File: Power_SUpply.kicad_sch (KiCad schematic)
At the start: 6 parts, among them J1 Conn_01x02, J2 Conn_01x02, U1 L7805

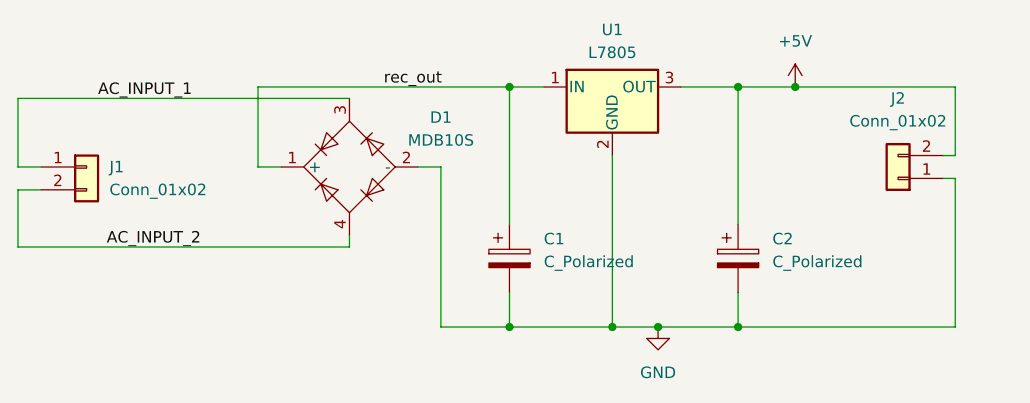
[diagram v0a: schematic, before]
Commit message: changed the connector
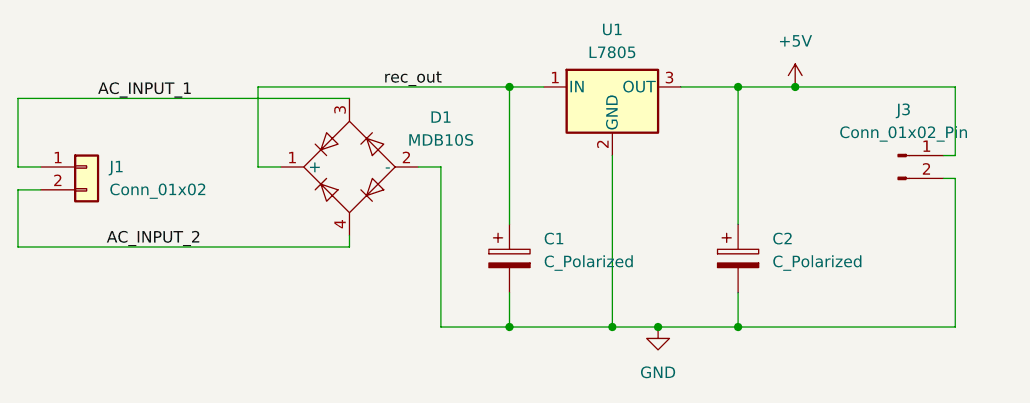
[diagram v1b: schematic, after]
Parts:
- removed J2: Conn_01x02, TerminalBlock_Phoenix:TerminalBlock_Phoenix_MKDS-1,5-2_1x02_P5.00mm_Horizontal, symbol Connector_Generic:Conn_01x02
- added J3: Conn_01x02_Pin, symbol Connector:Conn_01x02_Pin
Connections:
- net +5V: now also J3.1 (Pin_1)
- net GND: now also J3.2 (Pin_2)
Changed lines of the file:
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@@
-	)
-	(symbol
-		(lib_id "Connector_Generic:Conn_01x02")
-		(at 177.8 97.79 180)
-		(unit 1)
-		(exclude_from_sim no)
-		(in_bom yes)
-		(on_board yes)
-		(dnp no)
-		(fields_autoplaced yes)
-		(property "Reference" "J2"
-			(at 177.8 88.9 0)
-			(effects
-				(font
-					(size 1.27 1.27)
-				)
-			)
-		)
-		(property "Value" "Conn_01x02"
-			(at 177.8 91.44 0)
-			(effects
-				(font
-					(size 1.27 1.27)
-				)
-			)
-		)
-		(property "Footprint" "TerminalBlock_Phoenix:TerminalBlock_Phoenix_MKDS-1,5-2_1x02_P5.00mm_Horizontal"
-			(at 177.8 97.79 0)
-			(effects
-				(font
-					(size 1.27 1.27)
-				)
-				(hide yes)
-			)
-		)
-		(property "Datasheet" "~"
-			(at 177.8 97.79 0)
-			(effects
-				(font
-					(size 1.27 1.27)
-				)
-				(hide yes)
-			)
-		)
-		(property "Description" "Generic connector, single row, 01x02, script generated (kicad-library-utils/schlib/autogen/connector/)"
-			(at 177.8 97.79 0)
-			(effects
-				(font
-					(size 1.27 1.27)
-				)
-				(hide yes)
-			)
-		)
-		(pin "1"
-		)
-		(pin "2"
-		)
-		(instances
-			(project "Power_SUpply"
-				(path "/dd0fb984-5fbc-40cd-9654-8bc1b9a1f53d"
-					(reference "J2")
-					(unit 1)
-				)
-			)
-		)
 	)
 	(symbol
@@
 					(unit 1)
 				)
+			)
+		)
+	)
+	(symbol
+		(lib_id "Connector:Conn_01x02_Pin")
+		(at 177.8 95.25 0)
+		(unit 1)
+		(exclude_from_sim no)
+		(in_bom yes)
+		(on_board yes)
+		(dnp no)
+		(fields_autoplaced yes)
+		(property "Reference" "J3"
+			(at 178.435 90.17 0)
+			(effects
+				(font
+					(size 1.27 1.27)
+				)
+			)
+		)
+		(property "Value" "Conn_01x02_Pin"
+			(at 178.435 92.71 0)
+			(effects
+				(font
+					(size 1.27 1.27)
+				)
+			)
+		)
+		(property "Footprint" ""
+			(at 177.8 95.25 0)
+			(effects
+				(font
+					(size 1.27 1.27)
+				)
+				(hide yes)
+			)
+		)
+		(property "Datasheet" "~"
+			(at 177.8 95.25 0)
+			(effects
+				(font
+					(size 1.27 1.27)
+				)
+				(hide yes)
+			)
+		)
+		(property "Description" "Generic connector, single row, 01x02, script generated"
+			(at 177.8 95.25 0)
+			(effects
+				(font
+					(size 1.27 1.27)
+				)
+				(hide yes)
+			)
+		)
+		(pin "1"
+		)
+		(pin "2"
+		)
+		(instances
+			(project ""
+				(path "/dd0fb984-5fbc-40cd-9654-8bc1b9a1f53d"
+					(reference "J3")
+					(unit 1)
+				)

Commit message: changed connector to screw terminal
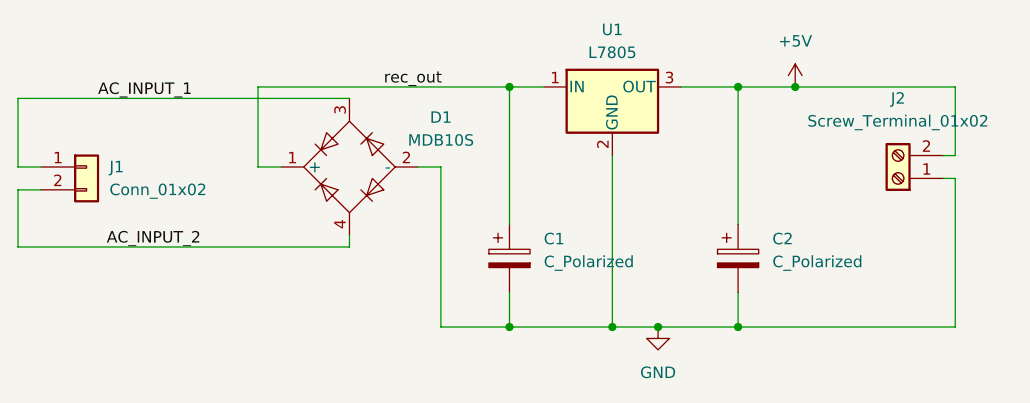
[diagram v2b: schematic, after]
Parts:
- removed J3: Conn_01x02_Pin, symbol Connector:Conn_01x02_Pin
- added J2: Screw_Terminal_01x02, symbol Connector:Screw_Terminal_01x02
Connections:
- net +5V: now also J2.2 (Pin_2)
- net GND: now also J2.1 (Pin_1)
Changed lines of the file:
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@@
-	)
-	(symbol
-		(lib_id "Connector:Conn_01x02_Pin")
-		(at 177.8 95.25 0)
-		(unit 1)
-		(exclude_from_sim no)
-		(in_bom yes)
-		(on_board yes)
-		(dnp no)
-		(fields_autoplaced yes)
-		(property "Reference" "J3"
-			(at 178.435 90.17 0)
-			(effects
-				(font
-					(size 1.27 1.27)
-				)
-			)
-		)
-		(property "Value" "Conn_01x02_Pin"
-			(at 178.435 92.71 0)
-			(effects
-				(font
-					(size 1.27 1.27)
-				)
-			)
-		)
-		(property "Footprint" ""
-			(at 177.8 95.25 0)
-			(effects
-				(font
-					(size 1.27 1.27)
-				)
-				(hide yes)
-			)
-		)
-		(property "Datasheet" "~"
-			(at 177.8 95.25 0)
-			(effects
-				(font
-					(size 1.27 1.27)
-				)
-				(hide yes)
-			)
-		)
-		(property "Description" "Generic connector, single row, 01x02, script generated"
-			(at 177.8 95.25 0)
-			(effects
-				(font
-					(size 1.27 1.27)
-				)
-				(hide yes)
-			)
-		)
-		(pin "1"
-		)
-		(pin "2"
-		)
-		(instances
-			(project ""
-				(path "/dd0fb984-5fbc-40cd-9654-8bc1b9a1f53d"
-					(reference "J3")
-					(unit 1)
-				)
-			)
-		)
 	)
 	(symbol
@@
 					(unit 1)
 				)
+			)
+		)
+	)
+	(symbol
+		(lib_id "Connector:Screw_Terminal_01x02")
+		(at 177.8 97.79 180)
+		(unit 1)
+		(exclude_from_sim no)
+		(in_bom yes)
+		(on_board yes)
+		(dnp no)
+		(fields_autoplaced yes)
+		(property "Reference" "J2"
+			(at 177.8 88.9 0)
+			(effects
+				(font
+					(size 1.27 1.27)
+				)
+			)
+		)
+		(property "Value" "Screw_Terminal_01x02"
+			(at 177.8 91.44 0)
+			(effects
+				(font
+					(size 1.27 1.27)
+				)
+			)
+		)
+		(property "Footprint" ""
+			(at 177.8 97.79 0)
+			(effects
+				(font
+					(size 1.27 1.27)
+				)
+				(hide yes)
+			)
+		)
+		(property "Datasheet" "~"
+			(at 177.8 97.79 0)
+			(effects
+				(font
+					(size 1.27 1.27)
+				)
+				(hide yes)
+			)
+		)
+		(property "Description" "Generic screw terminal, single row, 01x02, script generated (kicad-library-utils/schlib/autogen/connector/)"
+			(at 177.8 97.79 0)
+			(effects
+				(font
+					(size 1.27 1.27)
+				)
+				(hide yes)
+			)
+		)
+		(pin "1"
+		)
+		(pin "2"
+		)
+		(instances
+			(project ""
+				(path "/dd0fb984-5fbc-40cd-9654-8bc1b9a1f53d"
+					(reference "J2")
+					(unit 1)
+				)
